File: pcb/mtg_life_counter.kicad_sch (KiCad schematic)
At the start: 98 parts, among them J1 USB C 4907, J2 ICSP, J3 TP_UART, SW1 SW_SPST, SW2 SW_SPST, U1 ATmega328P-AU, U2 74HC595, U3 74HC595, U4 74HC595, U5 74HC595, U6 TPIC6B595, U7 TPIC6B595, U8 74HC165, Y1 16MHz

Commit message: wip on common cathode with transistors design
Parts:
- removed C10, C4, C5, C6, C7, C8, C9: 0.1uF, Capacitor_SMD:C_0805_2012Metric_Pad1.15x1.40mm_HandSolder, symbol Device:C_Small
- removed D1: KW4-S561CVB RED SMD, mtg_life_counter:KW4-S561xxB_SMD, symbol mtg_life_counter:KW4-S561CxB
- removed D2: KW4-S561CGB GREEN SMD, mtg_life_counter:KW4-S561xxB_SMD, symbol mtg_life_counter:KW4-S561CxB
- removed D3: KW4-S561CAB YELLOW SMD, mtg_life_counter:KW4-S561xxB_SMD, symbol mtg_life_counter:KW4-S561CxB
- removed D4: KW4-S561CBB BLUE SMD, mtg_life_counter:KW4-S561xxB_SMD, symbol mtg_life_counter:KW4-S561CxB
- removed E1, E2, E3, E4: Rotary_Encoder_Switch, mtg_life_counter:TT_EN11-HSB, symbol mtg_life_counter-rescue:Rotary_Encoder_Switch-Device
- removed R10, R11, R12, R13, R14, R15, R16, R17: 330, Resistor_SMD:R_0805_2012Metric_Pad1.15x1.40mm_HandSolder, symbol Device:R
- removed R20, R21, R22, R23, R24, R25, R26, R27: 10, Resistor_SMD:R_0805_2012Metric_Pad1.15x1.40mm_HandSolder, symbol Device:R
- removed R30, R31, R32, R33, R34, R35, R36, R37: 100, Resistor_SMD:R_0805_2012Metric_Pad1.15x1.40mm_HandSolder, symbol Device:R
- removed R4, R5, R50, R51, R52, R53, R54, R55, R56, R57: 10k, Resistor_SMD:R_0805_2012Metric_Pad1.15x1.40mm_HandSolder, symbol Device:R
- removed R40, R41, R42, R43, R44, R45, R46, R47: 390, Resistor_SMD:R_0805_2012Metric_Pad1.15x1.40mm_HandSolder, symbol Device:R
- removed U2, U3, U4, U5: 74HC595, Package_SO:SOIC-16_3.9x9.9mm_P1.27mm, symbol 74xx:74HC595
- removed U6, U7: TPIC6B595, Package_SO:SOIC-20W_7.5x12.8mm_P1.27mm, symbol mtg_life_counter:TPIC6B595
- removed U8: 74HC165, Package_SO:SOIC-16_3.9x9.9mm_P1.27mm, symbol mtg_life_counter:74HC165
- added B10: P4 DOWN, mtg_life_counter:B3F_12mm, symbol Switch:SW_Push
- added B3: P1 UP, mtg_life_counter:B3F_12mm, symbol Switch:SW_Push
- added B4: P1 DOWN, mtg_life_counter:B3F_12mm, symbol Switch:SW_Push
- added B5: P2 UP, mtg_life_counter:B3F_12mm, symbol Switch:SW_Push
- added B6: P2 DOWN, mtg_life_counter:B3F_12mm, symbol Switch:SW_Push
- added B7: P3 Up, mtg_life_counter:B3F_12mm, symbol Switch:SW_Push
- added B8: P3 DOWN, mtg_life_counter:B3F_12mm, symbol Switch:SW_Push
- added B9: P4 UP, mtg_life_counter:B3F_12mm, symbol Switch:SW_Push
- R2, R3: value 10k -> 100k
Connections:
- net GND: now also B10.2, B3.2, B4.2, B5.2, B6.2, B7.2, B8.2, B9.2
- net E1_SW: no longer names the net of U1.28 (PC5(SCL/ADC5))
- net E2_SW: no longer names the net of U1.25 (PC2(ADC2))
- net E3_SW: no longer names the net of U1.9 (PD5)
- net E4_SW: no longer names the net of U1.32 (PD2(INT0))
- net RESET_BTN renamed BTN_RESET
- net ROLL_BTN renamed BTN_ROLL
- new net BTN_P1_DN: B4.1
- new net BTN_P1_UP: B3.1
- new net BTN_P2_DN: B6.1
- new net BTN_P2_UP: B5.1
- new net BTN_P3_DN: B8.1
- new net BTN_P3_UP: B7.1
- new net BTN_P4_DN: B10.1
- new net BTN_P4_UP: B9.1
- no-connect marks 15 -> 13
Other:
- added sheet Player Four Display Bank - Blue (display4.kicad_sch)
- added sheet Player One Display Bank - Red (display1.kicad_sch)
- added sheet Player Three Display Bank - Yellow (display3.kicad_sch)
- added sheet Player Two Display Bank - Green (display2.kicad_sch)
- note added: "Player Up/Down Buttons"
- note removed: "Encoder Readback"
- note removed: "Seven Segement Displays"
- moved on the sheet: R2, R3

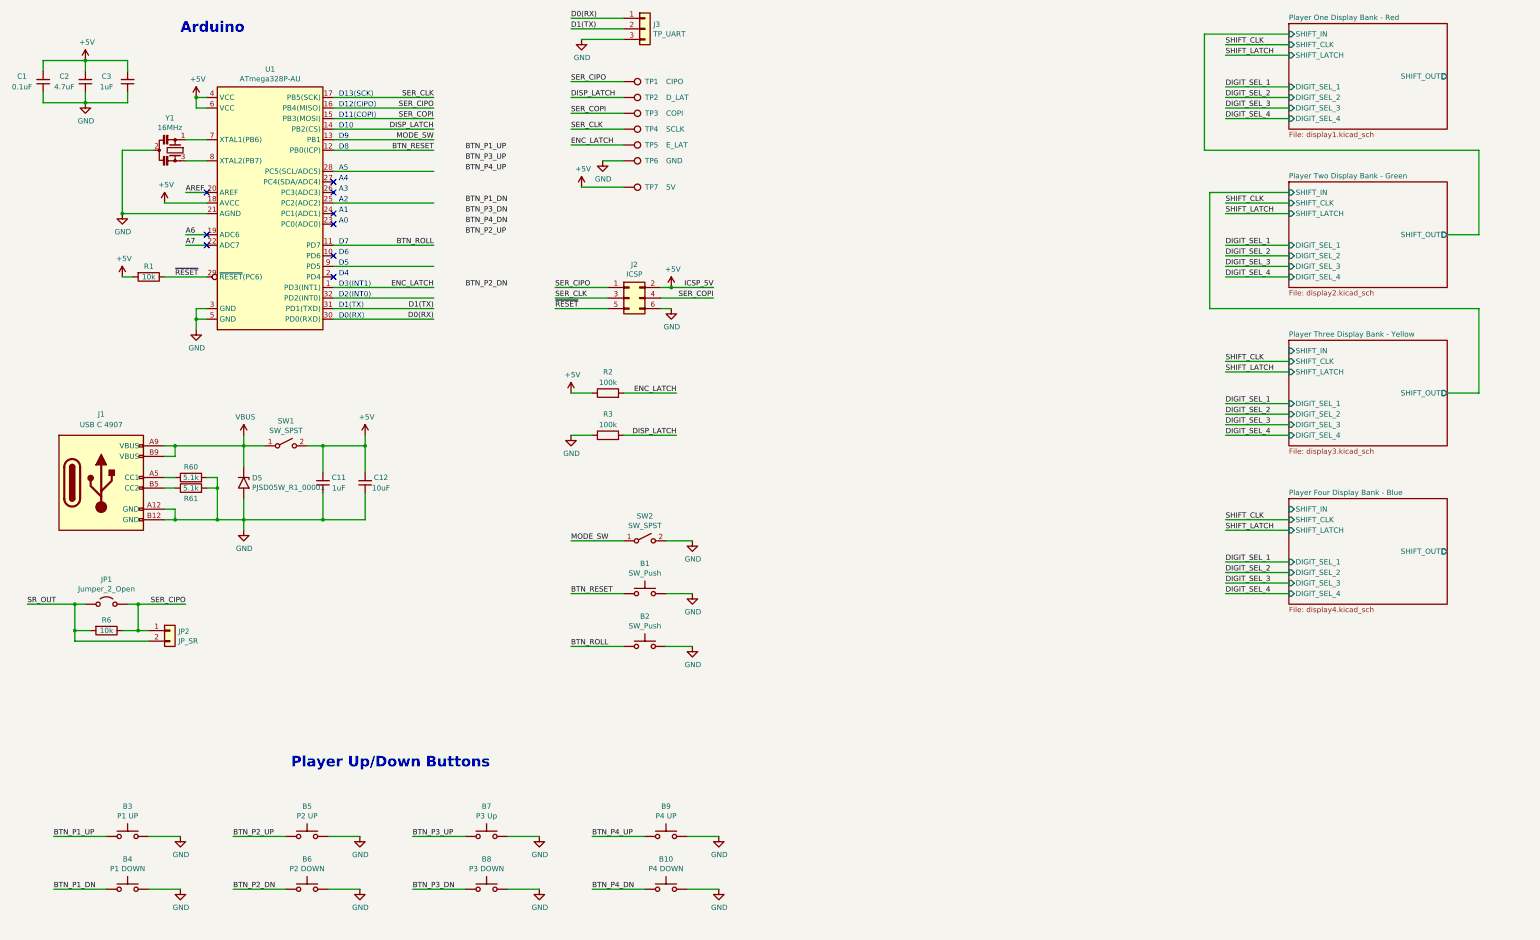
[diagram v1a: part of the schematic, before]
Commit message: tentative schematic for common cathode
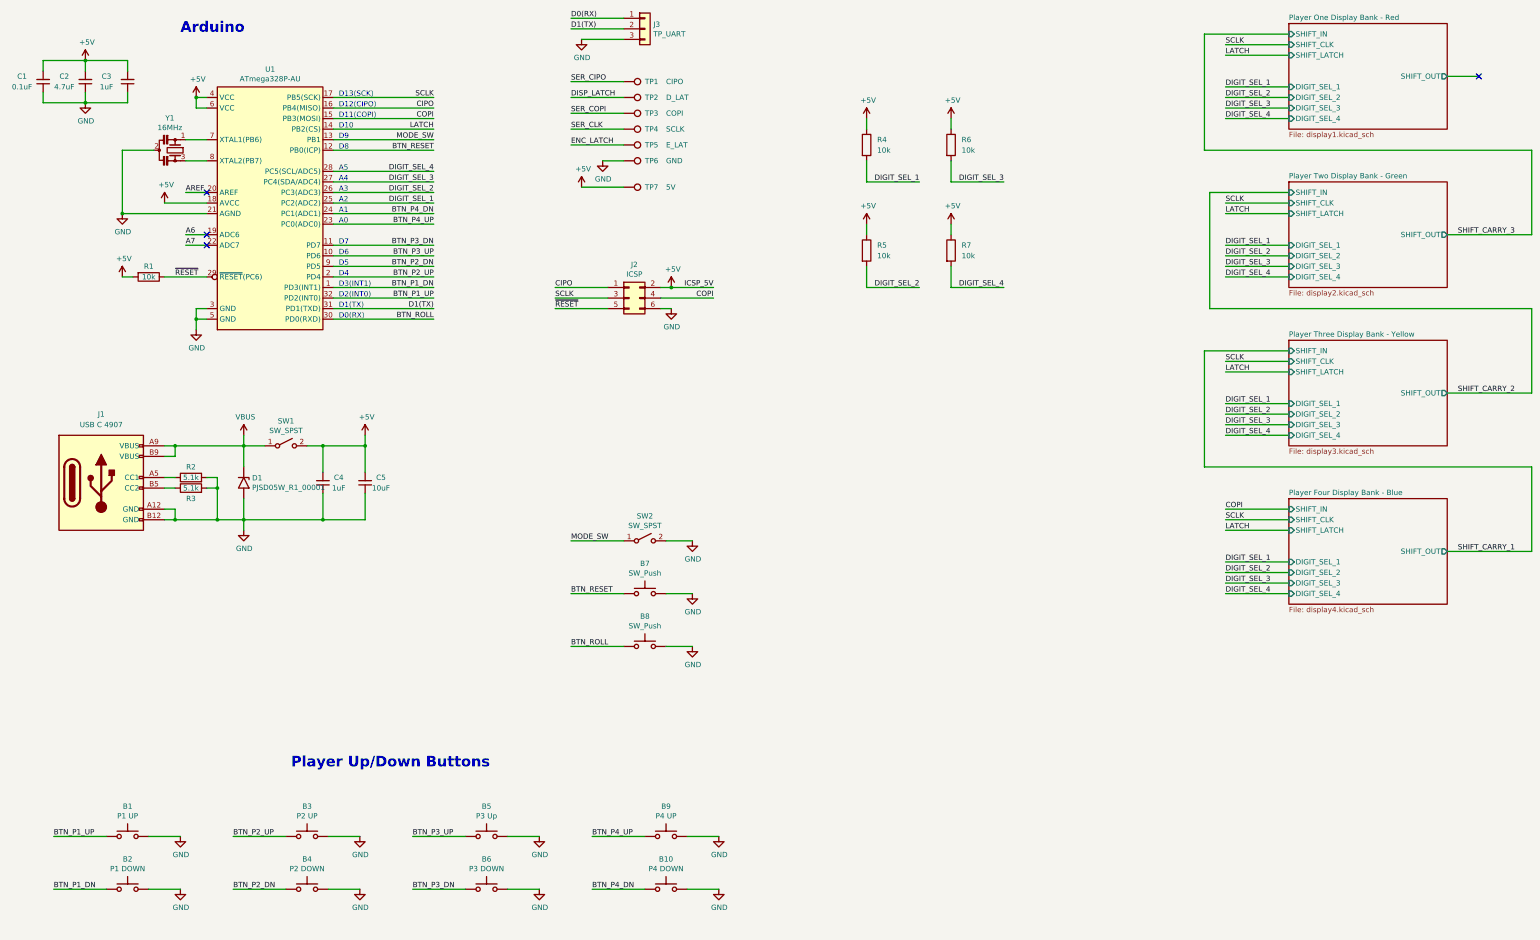
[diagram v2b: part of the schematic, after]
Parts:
- removed JP1: Jumper_2_Open, Jumper:SolderJumper-2_P1.3mm_Open_TrianglePad1.0x1.5mm, symbol Jumper:Jumper_2_Open
- removed JP2: JP_SR, mtg_life_counter:TP_Edge_2, symbol Connector_Generic:Conn_01x02
- removed R2, R3: 100k, Resistor_SMD:R_0805_2012Metric_Pad1.15x1.40mm_HandSolder, symbol Device:R
- added R4, R5, R7: 10k, Resistor_SMD:R_0805_2012Metric_Pad1.20x1.40mm_HandSolder, symbol Device:R
- C1, C2, C3: footprint Capacitor_SMD:C_0805_2012Metric_Pad1.15x1.40mm_HandSolder -> Capacitor_SMD:C_0805_2012Metric_Pad1.18x1.45mm_HandSolder
- C4: renamed from C11; footprint Capacitor_SMD:C_0805_2012Metric_Pad1.15x1.40mm_HandSolder -> Capacitor_SMD:C_0805_2012Metric_Pad1.18x1.45mm_HandSolder
- C5: renamed from C12; footprint Capacitor_SMD:C_0805_2012Metric_Pad1.15x1.40mm_HandSolder -> Capacitor_SMD:C_0805_2012Metric_Pad1.18x1.45mm_HandSolder
- R1, R6: footprint Resistor_SMD:R_0805_2012Metric_Pad1.15x1.40mm_HandSolder -> Resistor_SMD:R_0805_2012Metric_Pad1.20x1.40mm_HandSolder
- R2: renamed from R60; footprint Resistor_SMD:R_0805_2012Metric_Pad1.15x1.40mm_HandSolder -> Resistor_SMD:R_0805_2012Metric_Pad1.20x1.40mm_HandSolder
- R3: renamed from R61; footprint Resistor_SMD:R_0805_2012Metric_Pad1.15x1.40mm_HandSolder -> Resistor_SMD:R_0805_2012Metric_Pad1.20x1.40mm_HandSolder
- SW1, SW2: footprint Button_Switch_THT:SW_Slide_1P2T_CK_OS102011MS2Q -> Button_Switch_THT:SW_Slide_SPDT_Straight_CK_OS102011MS2Q
- Y1: footprint Crystal:Resonator_muRata_CSTLSxxxX-3Pin_W5.5mm_H3.0mm -> Crystal:Resonator_SMD-3Pin_7.2x3.0mm
- renumbered B3 to B1, B4 to B2, B5 to B3, B6 to B4, B7 to B5, B8 to B6, B1 to B7, B2 to B8, D5 to D1
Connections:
- net SR_OUT is gone; now on net DIGIT_SEL_3: R6.2
- net +5V: now also R6.1, R4.1, R5.1, R7.1
- net BTN_P1_DN: now also U1.1 (PD3(INT1))
- net BTN_P1_UP: now also U1.32 (PD2(INT0))
- net BTN_P2_DN: now also U1.9 (PD5)
- net BTN_P2_UP: now also U1.2 (PD4)
- net BTN_P3_DN: now also U1.11 (PD7)
- net BTN_P3_UP: now also U1.10 (PD6)
- net BTN_P4_DN: now also U1.24 (PC1(ADC1))
- net BTN_P4_UP: now also U1.23 (PC0(ADC0))
- net BTN_ROLL: now also U1.30 (PD0(RXD)); no longer U1.11 (PD7)
- net D0(RX): no longer U1.30 (PD0(RXD))
- net DIGIT_SEL_1: now also U1.25 (PC2(ADC2)), R4.2
- net DIGIT_SEL_2: now also U1.26 (PC3(ADC3)), R5.2
- net DIGIT_SEL_3: now also U1.27 (PC4(SDA/ADC4))
- net DIGIT_SEL_4: now also U1.28 (PC5(SCL/ADC5)), R7.2
- net DISP_LATCH: no longer U1.14 (PB2(CS))
- net ENC_LATCH: no longer U1.1 (PD3(INT1))
- net SER_CIPO: no longer J2.1 (Pin_1), R6.1, U1.16 (PB4(MISO))
- net SER_CLK: no longer J2.3 (Pin_3), U1.17 (PB5(SCK))
- net SER_COPI: no longer J2.4 (Pin_4), U1.15 (PB3(MOSI))
- new net CIPO: J2.1 (Pin_1), U1.16 (PB4(MISO))
- new net COPI: J2.4 (Pin_4), U1.15 (PB3(MOSI))
- new net LATCH: U1.14 (PB2(CS))
- new net SCLK: J2.3 (Pin_3), U1.17 (PB5(SCK))
- no-connect marks 13 -> 8

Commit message: common anode schematic
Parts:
- renumbered B8 to B10, B9 to B7, B10 to B8, B7 to B9
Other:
- moved on the sheet: B10, B9, SW2

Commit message: continue wip
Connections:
- net D0(RX): no longer names the net of J3.1 (Pin_1)
- net D1(TX) renamed TX
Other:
- sheet Player Four Display Bank - Blue renamed P4
- sheet Player One Display Bank - Red renamed P1
- sheet Player Three Display Bank - Yellow renamed P3
- sheet Player Two Display Bank - Green renamed P2
- note added: "Player 1 Display Bank - Red"
- note added: "Player 2 Display Bank - Green"
- note added: "Player 3 Display Bank - Yellow"
- note added: "Player 4 Display Bank - Blue"
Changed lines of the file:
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@@
 		)
 	)
+	(text "Player 2 Display Bank - Green"
+		(exclude_from_sim no)
+		(at 349.25 62.23 0)
+		(effects
+			(font
+				(size 1.27 1.27)
+			)
+		)
+	)
 	(text "A5"
 		(exclude_from_sim no)
@@
 		)
 	)
+	(text "Player 3 Display Bank - Yellow"
+		(exclude_from_sim no)
+		(at 350.52 100.33 0)
+		(effects
+			(font
+				(size 1.27 1.27)
+			)
+		)
+	)
 	(text "D12(CIPO)"
 		(exclude_from_sim no)
@@
 		)
 	)
+	(text "Player 4 Display Bank - Blue"
+		(exclude_from_sim no)
+		(at 350.52 138.43 0)
+		(effects
+			(font
+				(size 1.27 1.27)
+			)
+		)
+	)
 	(text "D7"
 		(exclude_from_sim no)
@@
 		)
 	)
+	(text "Player 1 Display Bank - Red"
+		(exclude_from_sim no)
+		(at 349.25 24.13 0)
+		(effects
+			(font
+				(size 1.27 1.27)
+			)
+		)
+	)
 	(text "D10"
 		(exclude_from_sim no)
@@
 		)
 	)
-	(label "D1(TX)"
+	(label "TX"
 		(at 124.46 93.98 180)
 		(effects
@@
 		)
 	)
-	(label "D1(TX)"
+	(label "TX"
 		(at 157.48 26.67 0)
 		(effects
@@
 		)
 	)
-	(label "D0(RX)"
-		(at 157.48 24.13 0)
-		(effects
-			(font
-				(size 1.27 1.27)
-			)
-			(justify left bottom)
-		)
-	)
 	(label "BTN_P3_DN"
 		(at 124.46 78.74 180)
@@
 			(color 0 0 0 0.0000)
 		)
-		(property "Sheetname" "Player Two Display Bank - Green"
+		(property "Sheetname" "P2"
 			(at 330.2 62.7884 0)
 			(effects
@@
 			(color 0 0 0 0.0000)
 		)
-		(property "Sheetname" "Player Four Display Bank - Blue"
+		(property "Sheetname" "P4"
 			(at 330.2 138.9884 0)
 			(effects
@@
 			(color 0 0 0 0.0000)
 		)
-		(property "Sheetname" "Player One Display Bank - Red"
+		(property "Sheetname" "P1"
 			(at 330.2 24.6884 0)
 			(effects
@@
 			(color 0 0 0 0.0000)
 		)
-		(property "Sheetname" "Player Three Display Bank - Yellow"
+		(property "Sheetname" "P3"
 			(at 330.2 100.8884 0)
 			(effects
